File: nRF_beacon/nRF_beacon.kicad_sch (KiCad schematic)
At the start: 0 parts

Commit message: Lagt inn referanselayout for nRF54L15 (unntatt antenne matching network)
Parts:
- added C1: 10uF, symbol Device:C_Small
- added C2, C3, C4, C5: 100nF, symbol Device:C_Small
- added C6: 2.2uF, symbol Device:C_Small
- added C7: 3.9pF, symbol Device:C_Small
- added L1: 4.7uH, symbol Device:L_Small
- added R1: 1k, symbol Device:R_Small
- added U1: nRF54L15, symbol Ekse:nRF54L15
- added X1: 32MHz, symbol Device:Crystal_Small
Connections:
- new net: C6.1, L1.1, U1.45 (DECD)
- new net: L1.2, U1.46 (DCC)
- new net: C7.1, R1.1, U1.30 (~{RESET})
- new net Earth: C1.2, C2.2, C3.2, C4.2, C5.2, C6.2, C7.2
- new net SWDCLK: U1.26 (SWDCLK)
- new net SWDIO: U1.25 (SWDIO)
- new net VDD_nRF: C1.1, C2.1, C3.1, C4.1, C5.1, U1.10 (VDD), U1.22 (VDD), U1.36 (VDD), U1.47 (VDD), U1.48 (VDD)
- new net XC1: U1.34 (XC1), X1.2
- new net XC2: U1.35 (XC2), X1.1
- new net ~{RESET}: R1.2
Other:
- note added: "0201"
- note added: "0402"
- note added: "XTAL_2016"

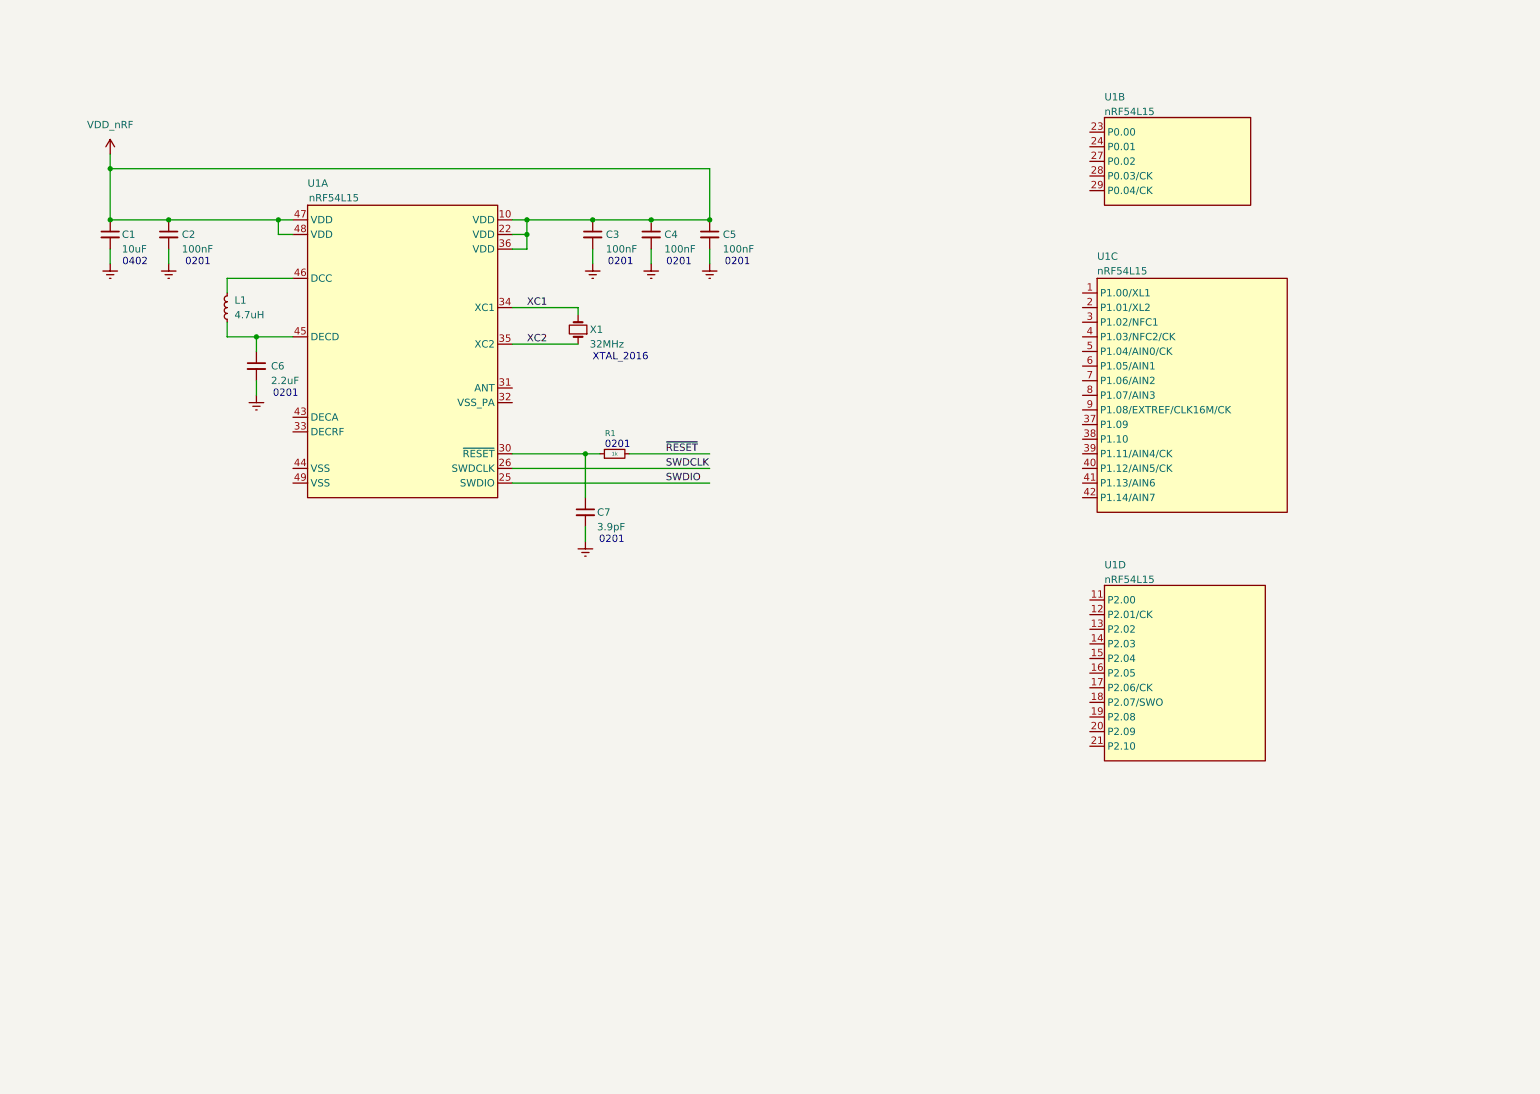
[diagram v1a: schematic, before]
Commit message: Added I2S audio interface schematic
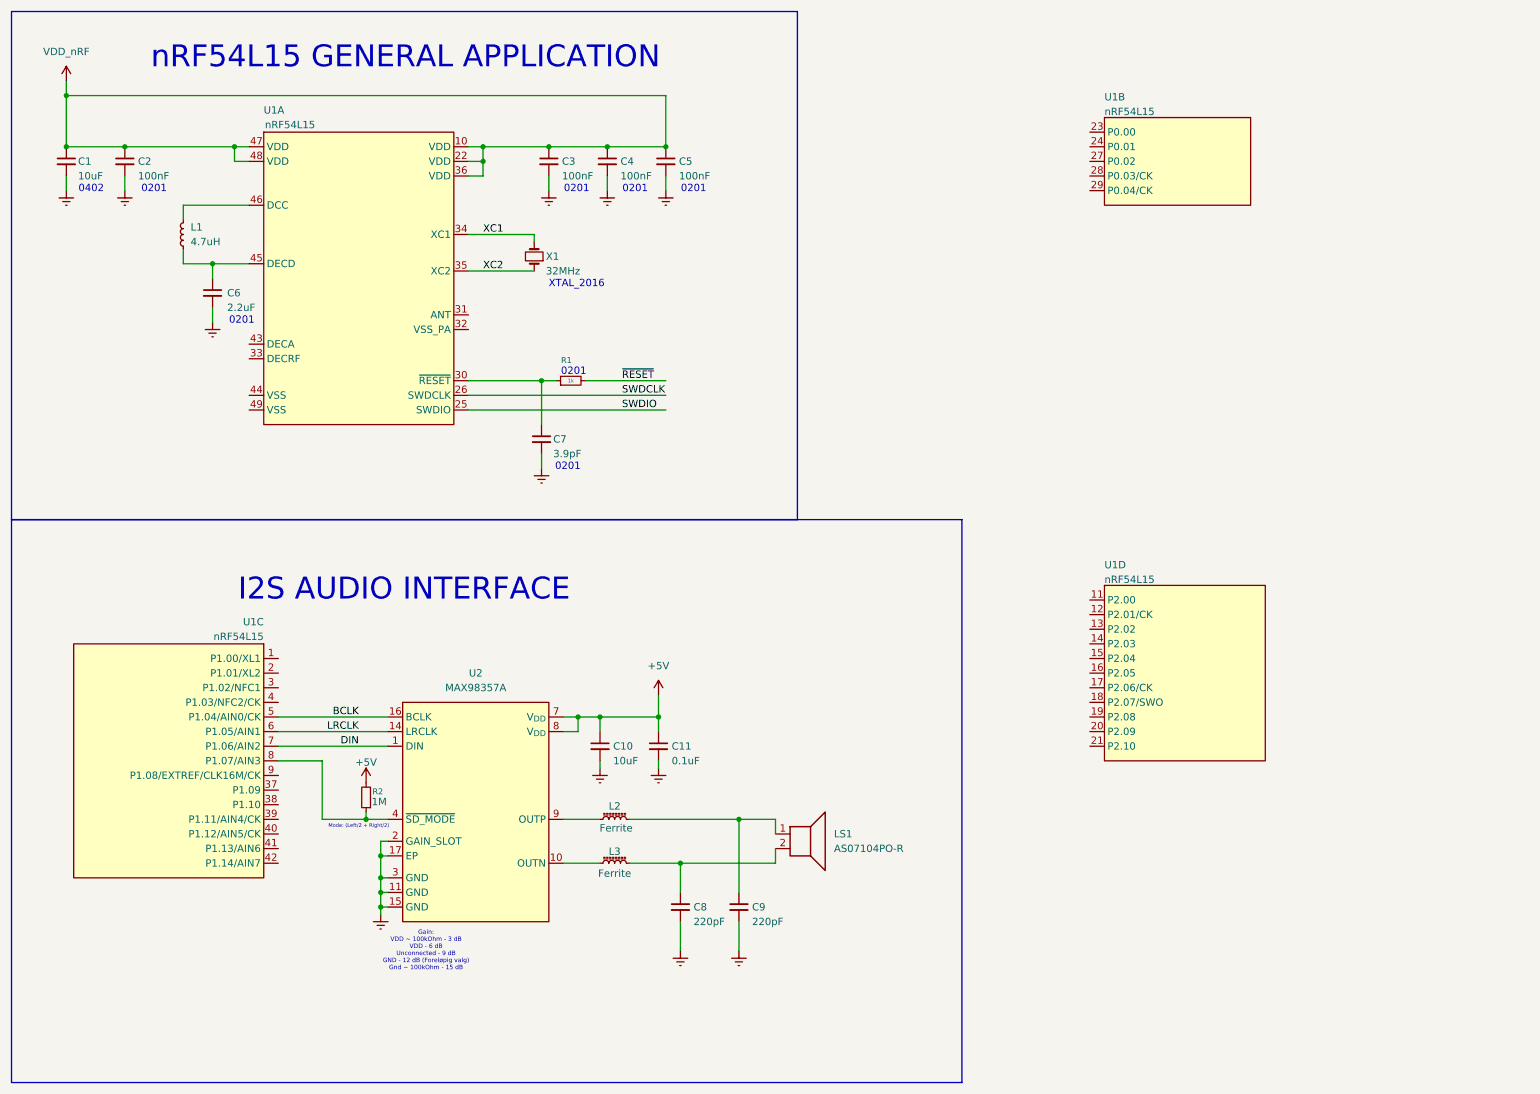
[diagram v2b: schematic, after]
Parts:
- added C10: 10uF, symbol Device:C_Small
- added C11: 0.1uF, symbol Device:C_Small
- added C8, C9: 220pF, symbol Device:C_Small
- added L2, L3: Ferrite, symbol Device:L_Ferrite_Small
- added LS1: AS07104PO-R, symbol Device:Speaker
- added R2: 1M, symbol Device:R_Small
- added U2: MAX98357A, Ekse:TQFN-16-1EP_3x3mm_P0.5mm_EP1.6x1.6mm, symbol Ekse:MAX98357A
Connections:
- net Earth: now also C10.2, C11.2, C8.2, C9.2, U2.11 (GND), U2.15 (GND), U2.17 (EP), U2.2 (GAIN_SLOT), U2.3 (GND)
- net BCLK: now reaches U1.5 (P1.04/AIN0/CK)
- net BCLK: now also U2.16 (BCLK)
- net LRCLK: now reaches U1.6 (P1.05/AIN1)
- net LRCLK: now also U2.14 (LRCLK)
- net DIN: now reaches U1.7 (P1.06/AIN2)
- net DIN: now also U2.1 (DIN)
- net at U1.8 (P1.07/AIN3): now also R2.1, U2.4 (~{SD_MODE})
- new net: C8.1, L3.2, LS1.2
- new net: L3.1, U2.10 (OUTN)
- new net: L2.1, U2.9 (OUTP)
- new net: C9.1, L2.2, LS1.1
- new net +5V: C10.1, C11.1, R2.2, U2.7 (V_{DD}), U2.8 (V_{DD})
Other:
- note added: "Gain: VDD ~ 100kOhm - 3 dB VDD - 6 dB Unconnected - 9 dB GND - 12 dB (Foreløpig valg) Gnd ~ 100kOhm - 15 dB"
- note added: "I2S AUDIO INTERFACE"
- note added: "Mode: (Left/2 + Right/2)"
- note added: "nRF54L15 GENERAL APPLICATION"
- moved on the sheet: C1, C2, C3, C4, C5, C6, C7, L1, R1, U1A, U1C, X1

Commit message: Added footprint and model for nRF and nPM
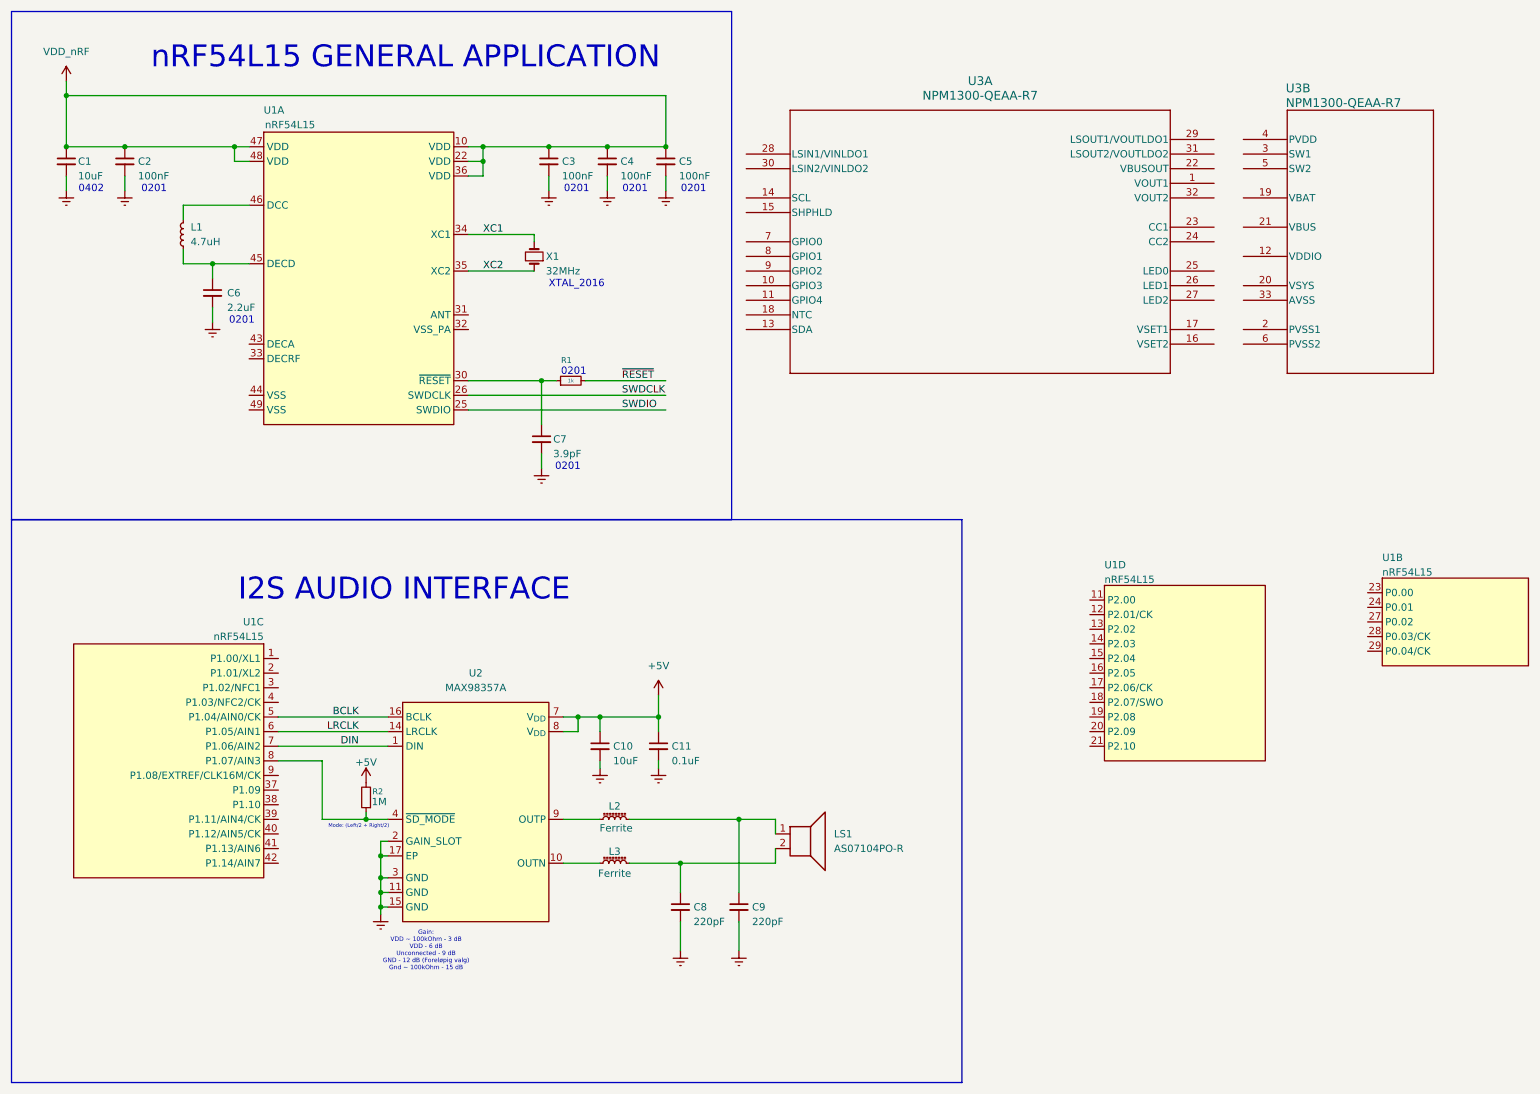
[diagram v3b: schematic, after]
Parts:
- added U3: NPM1300-QEAA-R7, Ekse:QFN32_5X5_NOR, symbol Ekse:NPM1300-QEAA-R7
- U1: footprint (none) -> Ekse:QFN48_6X6_NOR
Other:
- moved on the sheet: U1B

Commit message: Created new symbol for nPM1300
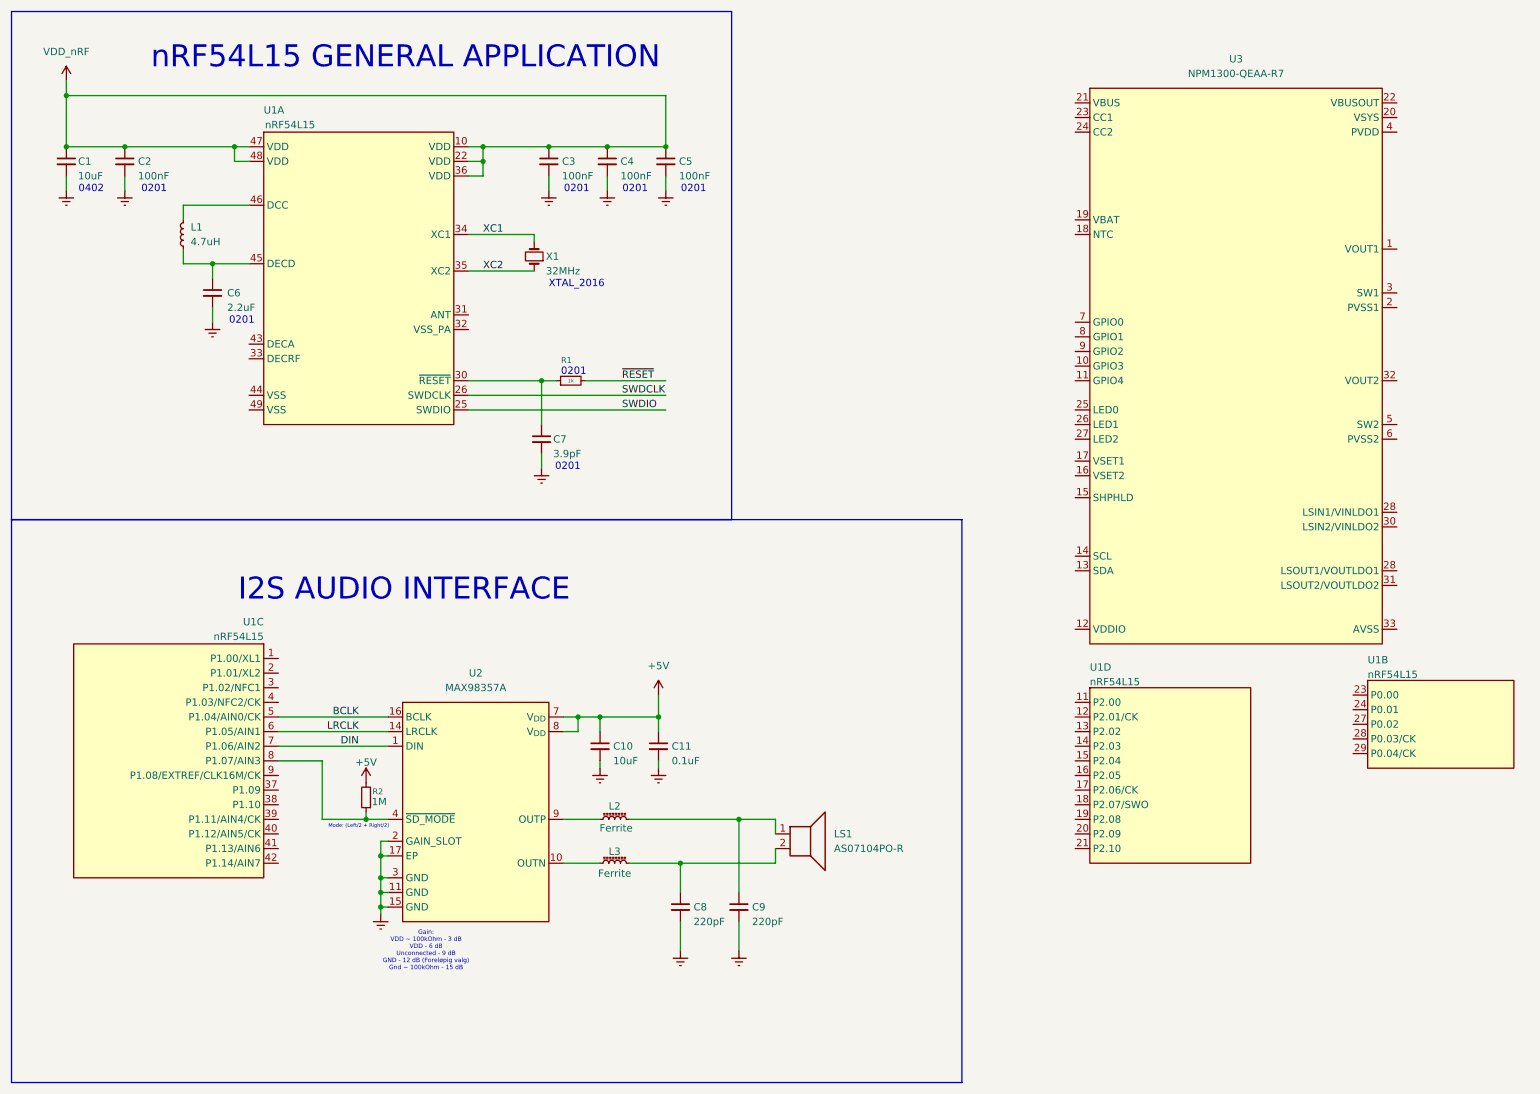
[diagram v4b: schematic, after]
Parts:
- removed unit 2 of U3
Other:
- moved on the sheet: U1B, U1D

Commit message: Added hierchical sheets for simple block diagram on root page, with complex circuits on their own page
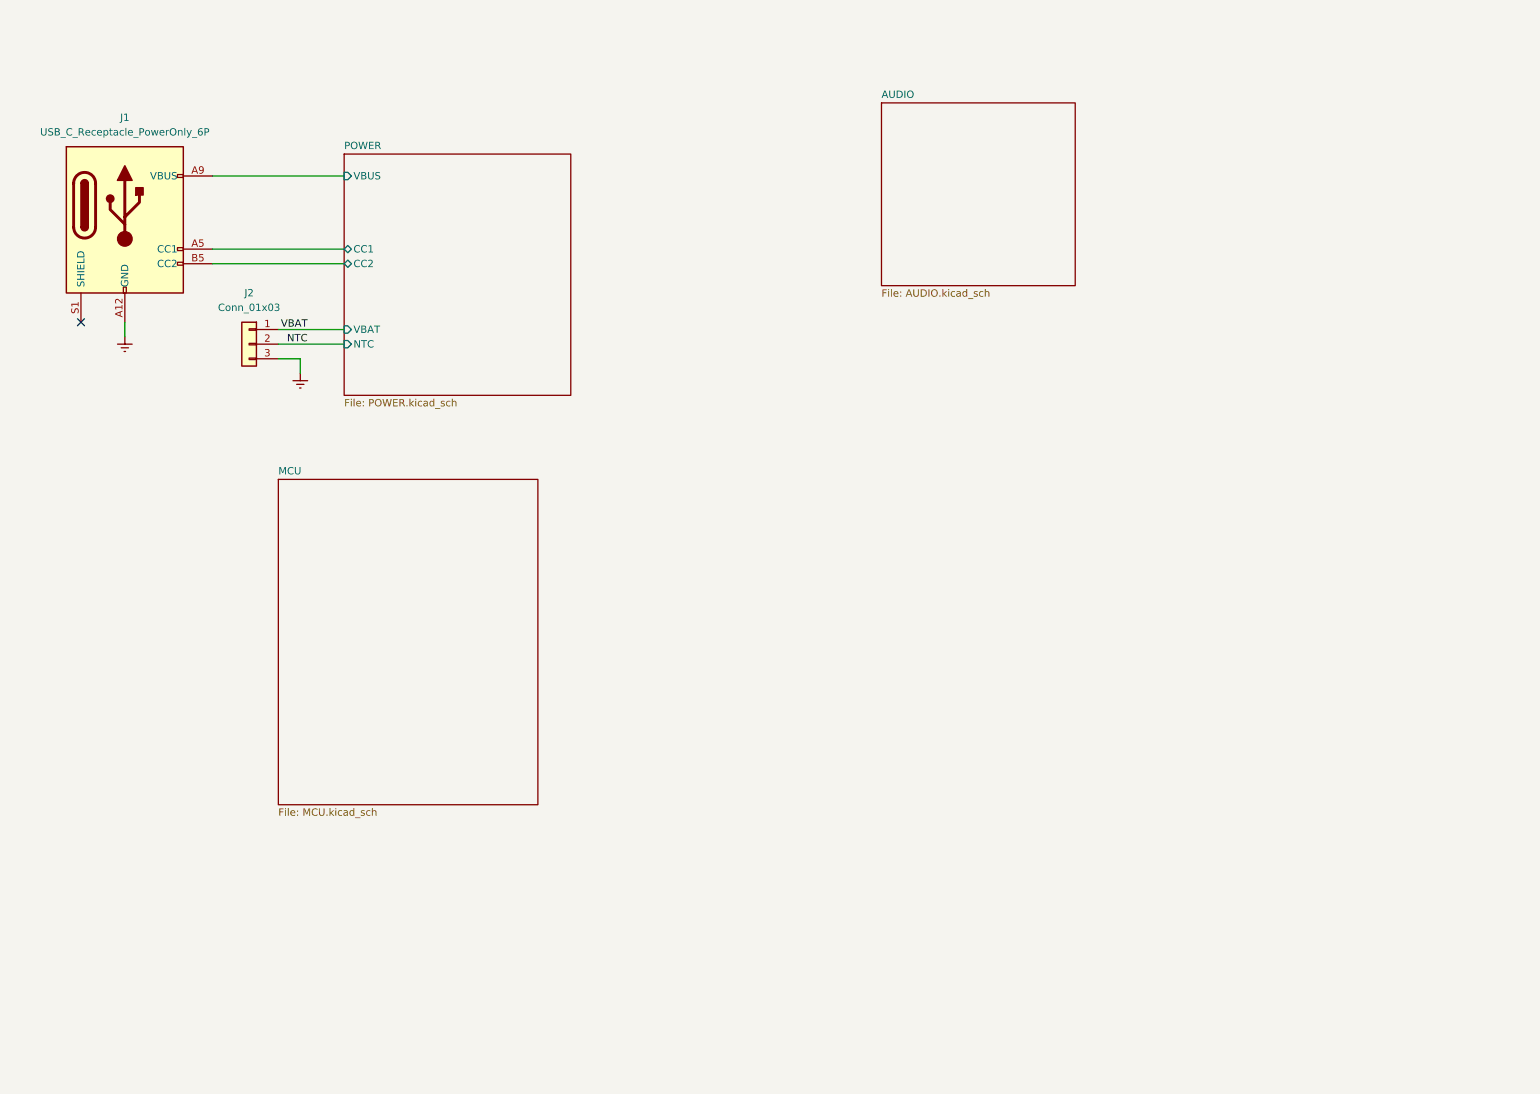
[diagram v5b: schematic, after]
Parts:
- removed C1, C10: 10uF, symbol Device:C_Small
- removed C11: 0.1uF, symbol Device:C_Small
- removed C2, C3, C4, C5: 100nF, symbol Device:C_Small
- removed C6: 2.2uF, symbol Device:C_Small
- removed C7: 3.9pF, symbol Device:C_Small
- removed C8, C9: 220pF, symbol Device:C_Small
- removed L1: 4.7uH, symbol Device:L_Small
- removed L2, L3: Ferrite, symbol Device:L_Ferrite_Small
- removed LS1: AS07104PO-R, symbol Device:Speaker
- removed R1: 1k, symbol Device:R_Small
- removed R2: 1M, symbol Device:R_Small
- removed U1: nRF54L15, Ekse:QFN48_6X6_NOR, symbol Ekse:nRF54L15
- removed U2: MAX98357A, Ekse:TQFN-16-1EP_3x3mm_P0.5mm_EP1.6x1.6mm, symbol Ekse:MAX98357A
- removed U3: NPM1300-QEAA-R7, Ekse:QFN32_5X5_NOR, symbol Ekse:NPM1300-QEAA-R7
- removed X1: 32MHz, symbol Device:Crystal_Small
- added J1: USB_C_Receptacle_PowerOnly_6P, symbol Connector:USB_C_Receptacle_PowerOnly_6P
- added J2: Conn_01x03, symbol Connector_Generic:Conn_01x03
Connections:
- net Earth: now also J1.A12 (GND), J1.B12 (GND), J2.3 (Pin_3)
- new net NTC: J2.2 (Pin_2)
- new net POWER/CC1: J1.A5 (CC1)
- new net POWER/CC2: J1.B5 (CC2)
- new net POWER/VBUS: J1.A9 (VBUS), J1.B9 (VBUS)
- new net VBAT: J2.1 (Pin_1)
- no-connect marks 0 -> 1
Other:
- added sheet AUDIO (AUDIO.kicad_sch)
- added sheet MCU (MCU.kicad_sch)
- added sheet POWER (POWER.kicad_sch)
- note removed: "0201"
- note removed: "0402"
- note removed: "Gain: VDD ~ 100kOhm - 3 dB VDD - 6 dB Unconnected - 9 dB GND - 12 dB (Foreløpig valg) Gnd ~ 100kOhm - 15 dB"
- note removed: "I2S AUDIO INTERFACE"
- note removed: "Mode: (Left/2 + Right/2)"
- note removed: "XTAL_2016"
- note removed: "nRF54L15 GENERAL APPLICATION"
